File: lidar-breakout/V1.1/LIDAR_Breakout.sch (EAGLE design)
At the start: 88 parts, among them J1 UX60-MB-5S8, J2 AVR_SPI_PROG_3X2TESTPOINTS, P1 MOLEX 0436500200, X1 TSX-3225 16.0000MF18X-AC0

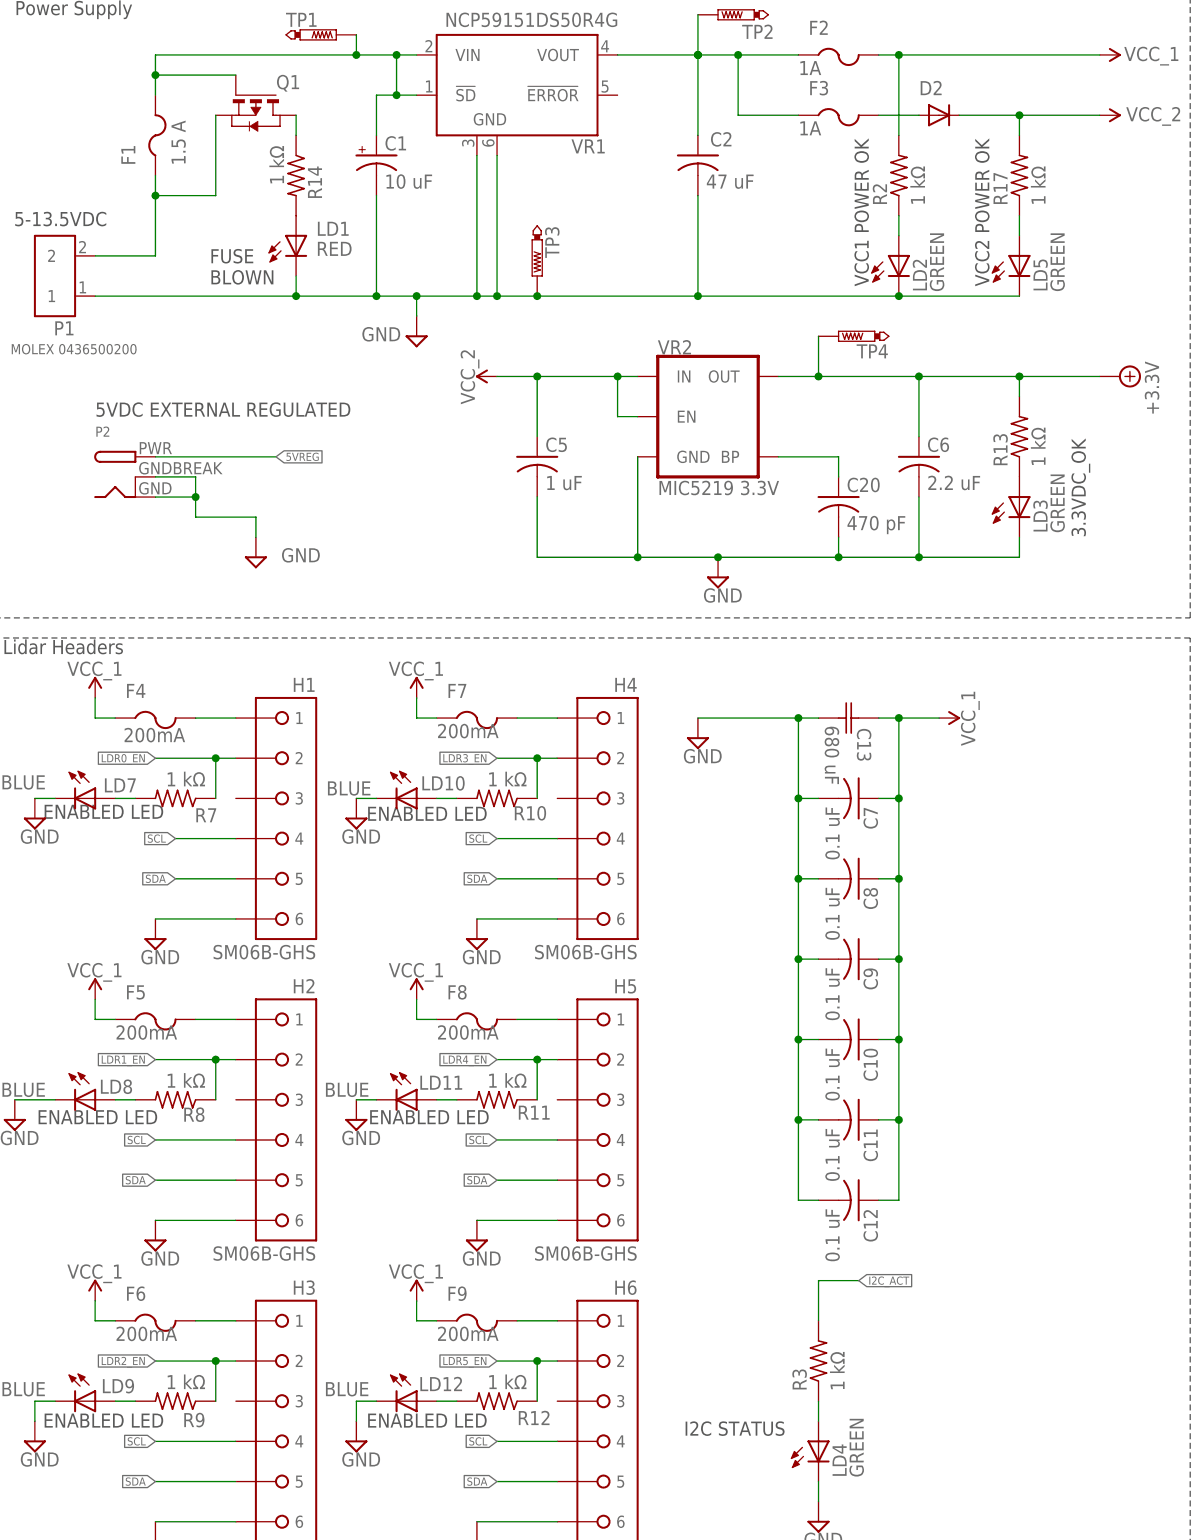
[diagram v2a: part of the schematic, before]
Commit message: Updated LED resistor values
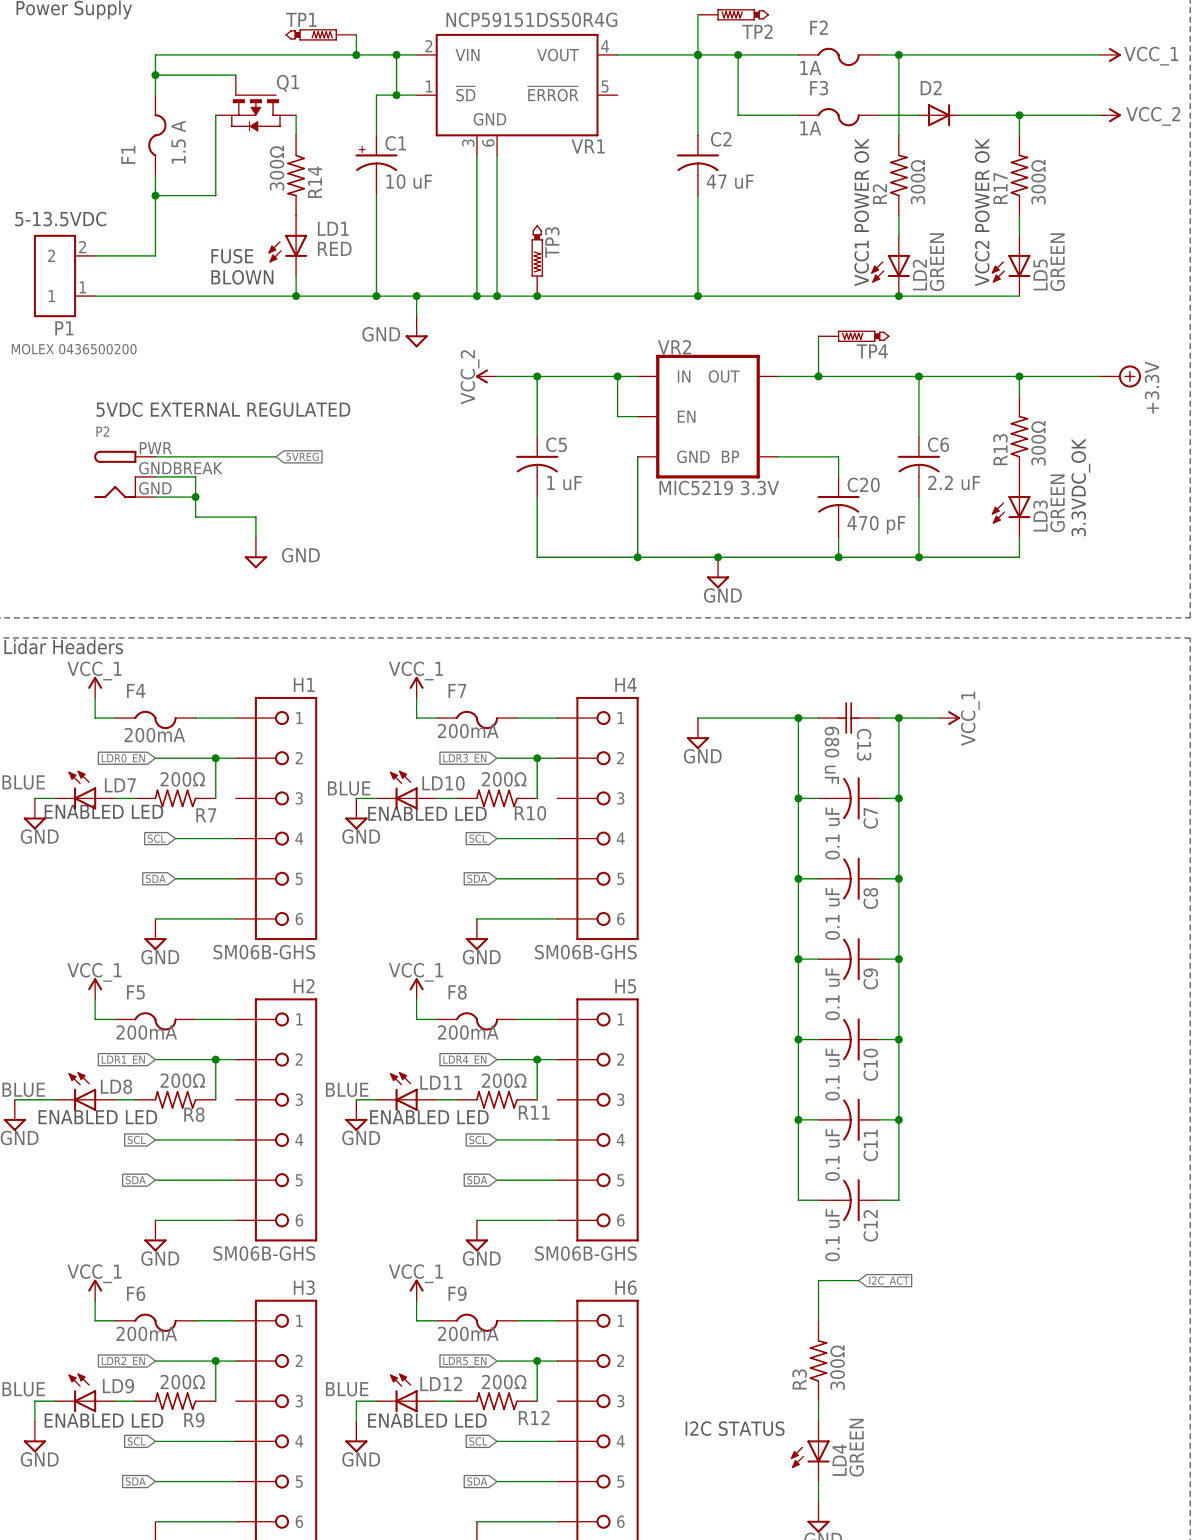
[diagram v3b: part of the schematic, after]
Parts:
- R10, R11, R12, R7, R8, R9: value 1 kΩ -> 200Ω
- R13, R14, R17, R2, R3: value 1 kΩ -> 300Ω
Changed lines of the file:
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@@
 <part name="C4" library="resistor" library_urn="urn:adsk.eagle:library:348" deviceset="C-US" device="C0603" package3d_urn="urn:adsk.eagle:package:26138/1" value="9 pF"/>
 <part name="LD2" library="led" library_urn="urn:adsk.eagle:library:259" deviceset="LED" device="CHIP-LED0603" package3d_urn="urn:adsk.eagle:package:15819/3" value="GREEN"/>
-<part name="R2" library="rcl" library_urn="urn:adsk.eagle:library:334" deviceset="R-US_" device="R0603" package3d_urn="urn:adsk.eagle:package:23555/2" value="1 kΩ"/>
+<part name="R2" library="rcl" library_urn="urn:adsk.eagle:library:334" deviceset="R-US_" device="R0603" package3d_urn="urn:adsk.eagle:package:23555/2" value="300Ω"/>
 <part name="FRAME1" library="CarWarsPCBv_3" deviceset="FRAME_B_L" device="">
 <attribute name="SCH_DESC" value="LIDAR LITE V3 INTERFACE BOARD"/>
@@
 <part name="R16" library="rcl" library_urn="urn:adsk.eagle:library:334" deviceset="R-US_" device="R0603" package3d_urn="urn:adsk.eagle:package:23555/2" value="22 Ω"/>
 <part name="LD1" library="RoboJackets-LEDs" deviceset="LED-SMD" device="" technology="-RED" value="RED"/>
-<part name="R14" library="rcl" library_urn="urn:adsk.eagle:library:334" deviceset="R-US_" device="R0603" package3d_urn="urn:adsk.eagle:package:23555/2" value="1 kΩ"/>
+<part name="R14" library="rcl" library_urn="urn:adsk.eagle:library:334" deviceset="R-US_" device="R0603" package3d_urn="urn:adsk.eagle:package:23555/2" value="300Ω"/>
 <part name="C2" library="rcl" library_urn="urn:adsk.eagle:library:334" deviceset="C-US" device="C0805" package3d_urn="urn:adsk.eagle:package:23617/2" value="47 uF"/>
 <part name="SUPPLY37" library="supply2" library_urn="urn:adsk.eagle:library:372" deviceset="GND" device=""/>
@@
 <part name="SUPPLY30" library="supply2" library_urn="urn:adsk.eagle:library:372" deviceset="GND" device=""/>
 <part name="C21" library="resistor" library_urn="urn:adsk.eagle:library:348" deviceset="C-US" device="C0603" package3d_urn="urn:adsk.eagle:package:26138/1" value="0.1 uF"/>
-<part name="R13" library="rcl" library_urn="urn:adsk.eagle:library:334" deviceset="R-US_" device="R0603" package3d_urn="urn:adsk.eagle:package:23555/2" value="1 kΩ"/>
+<part name="R13" library="rcl" library_urn="urn:adsk.eagle:library:334" deviceset="R-US_" device="R0603" package3d_urn="urn:adsk.eagle:package:23555/2" value="300Ω"/>
 <part name="LD3" library="led" library_urn="urn:adsk.eagle:library:259" deviceset="LED" device="CHIP-LED0603" package3d_urn="urn:adsk.eagle:package:15819/3" value="GREEN"/>
 <part name="D1" library="RoboJackets-Diodes" deviceset="DIODE-" device="DO-214AC"/>
@@
 <part name="R4" library="rcl" library_urn="urn:adsk.eagle:library:334" deviceset="R-US_" device="R0603" package3d_urn="urn:adsk.eagle:package:23555/2" value="10 kΩ"/>
 <part name="PB2" library="RoboJackets-Switches" deviceset="RESET_PB_RA" device="" value="ETH_RESET"/>
-<part name="R7" library="rcl" library_urn="urn:adsk.eagle:library:334" deviceset="R-US_" device="R0603" package3d_urn="urn:adsk.eagle:package:23555/2" value="1 kΩ"/>
+<part name="R7" library="rcl" library_urn="urn:adsk.eagle:library:334" deviceset="R-US_" device="R0603" package3d_urn="urn:adsk.eagle:package:23555/2" value="200Ω"/>
 <part name="LD7" library="led" library_urn="urn:adsk.eagle:library:259" deviceset="LED" device="CHIP-LED0603" package3d_urn="urn:adsk.eagle:package:15819/3" value="BLUE"/>
 <part name="SUPPLY16" library="supply2" library_urn="urn:adsk.eagle:library:372" deviceset="GND" device=""/>
-<part name="R8" library="rcl" library_urn="urn:adsk.eagle:library:334" deviceset="R-US_" device="R0603" package3d_urn="urn:adsk.eagle:package:23555/2" value="1 kΩ"/>
+<part name="R8" library="rcl" library_urn="urn:adsk.eagle:library:334" deviceset="R-US_" device="R0603" package3d_urn="urn:adsk.eagle:package:23555/2" value="200Ω"/>
 <part name="LD8" library="led" library_urn="urn:adsk.eagle:library:259" deviceset="LED" device="CHIP-LED0603" package3d_urn="urn:adsk.eagle:package:15819/3" value="BLUE"/>
 <part name="SUPPLY17" library="supply2" library_urn="urn:adsk.eagle:library:372" deviceset="GND" device=""/>
-<part name="R9" library="rcl" library_urn="urn:adsk.eagle:library:334" deviceset="R-US_" device="R0603" package3d_urn="urn:adsk.eagle:package:23555/2" value="1 kΩ"/>
-<part name="R10" library="rcl" library_urn="urn:adsk.eagle:library:334" deviceset="R-US_" device="R0603" package3d_urn="urn:adsk.eagle:package:23555/2" value="1 kΩ"/>
-<part name="R11" library="rcl" library_urn="urn:adsk.eagle:library:334" deviceset="R-US_" device="R0603" package3d_urn="urn:adsk.eagle:package:23555/2" value="1 kΩ"/>
-<part name="R12" library="rcl" library_urn="urn:adsk.eagle:library:334" deviceset="R-US_" device="R0603" package3d_urn="urn:adsk.eagle:package:23555/2" value="1 kΩ"/>
+<part name="R9" library="rcl" library_urn="urn:adsk.eagle:library:334" deviceset="R-US_" device="R0603" package3d_urn="urn:adsk.eagle:package:23555/2" value="200Ω"/>
+<part name="R10" library="rcl" library_urn="urn:adsk.eagle:library:334" deviceset="R-US_" device="R0603" package3d_urn="urn:adsk.eagle:package:23555/2" value="200Ω"/>
+<part name="R11" library="rcl" library_urn="urn:adsk.eagle:library:334" deviceset="R-US_" device="R0603" package3d_urn="urn:adsk.eagle:package:23555/2" value="200Ω"/>
+<part name="R12" library="rcl" library_urn="urn:adsk.eagle:library:334" deviceset="R-US_" device="R0603" package3d_urn="urn:adsk.eagle:package:23555/2" value="200Ω"/>
 <part name="LD9" library="led" library_urn="urn:adsk.eagle:library:259" deviceset="LED" device="CHIP-LED0603" package3d_urn="urn:adsk.eagle:package:15819/3" value="BLUE"/>
 <part name="SUPPLY18" library="supply2" library_urn="urn:adsk.eagle:library:372" deviceset="GND" device=""/>
@@
 <part name="SUPPLY31" library="SparkFun-PowerSymbols" library_urn="urn:adsk.eagle:library:530" deviceset="VCC_2" device=""/>
 <part name="LD4" library="led" library_urn="urn:adsk.eagle:library:259" deviceset="LED" device="CHIP-LED0603" package3d_urn="urn:adsk.eagle:package:15819/3" value="GREEN"/>
-<part name="R3" library="rcl" library_urn="urn:adsk.eagle:library:334" deviceset="R-US_" device="R0603" package3d_urn="urn:adsk.eagle:package:23555/2" value="1 kΩ"/>
+<part name="R3" library="rcl" library_urn="urn:adsk.eagle:library:334" deviceset="R-US_" device="R0603" package3d_urn="urn:adsk.eagle:package:23555/2" value="300Ω"/>
 <part name="SUPPLY5" library="supply2" library_urn="urn:adsk.eagle:library:372" deviceset="GND" device=""/>
 <part name="SUPPLY8" library="supply2" library_urn="urn:adsk.eagle:library:372" deviceset="GND" device=""/>
@@
 <part name="SUPPLY15" library="SparkFun-PowerSymbols" library_urn="urn:adsk.eagle:library:530" deviceset="VCC_2" device=""/>
 <part name="SUPPLY9" library="SparkFun-PowerSymbols" library_urn="urn:adsk.eagle:library:530" deviceset="VCC_2" device=""/>
-<part name="R17" library="rcl" library_urn="urn:adsk.eagle:library:334" deviceset="R-US_" device="R0603" package3d_urn="urn:adsk.eagle:package:23555/2" value="1 kΩ"/>
+<part name="R17" library="rcl" library_urn="urn:adsk.eagle:library:334" deviceset="R-US_" device="R0603" package3d_urn="urn:adsk.eagle:package:23555/2" value="300Ω"/>
 <part name="LD5" library="led" library_urn="urn:adsk.eagle:library:259" deviceset="LED" device="CHIP-LED0603" package3d_urn="urn:adsk.eagle:package:15819/3" value="GREEN"/>
 <part name="J1" library="RoboJackets-Connectors" deviceset="UX60*-MB-5S?" device="8"/>
